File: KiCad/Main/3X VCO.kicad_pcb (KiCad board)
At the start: 2 copper layers, 99.6 x 99.8 mm, 92 parts, among them J1 Conn_01x32_Socket, J2 Conn_02x05_Odd_Even, J3 Conn_01x32_Socket, Q1 BC558, Q2 BC548, Q3 BC558, Q4 BC548, Q5 BC558, Q6 BC548, U1 40106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

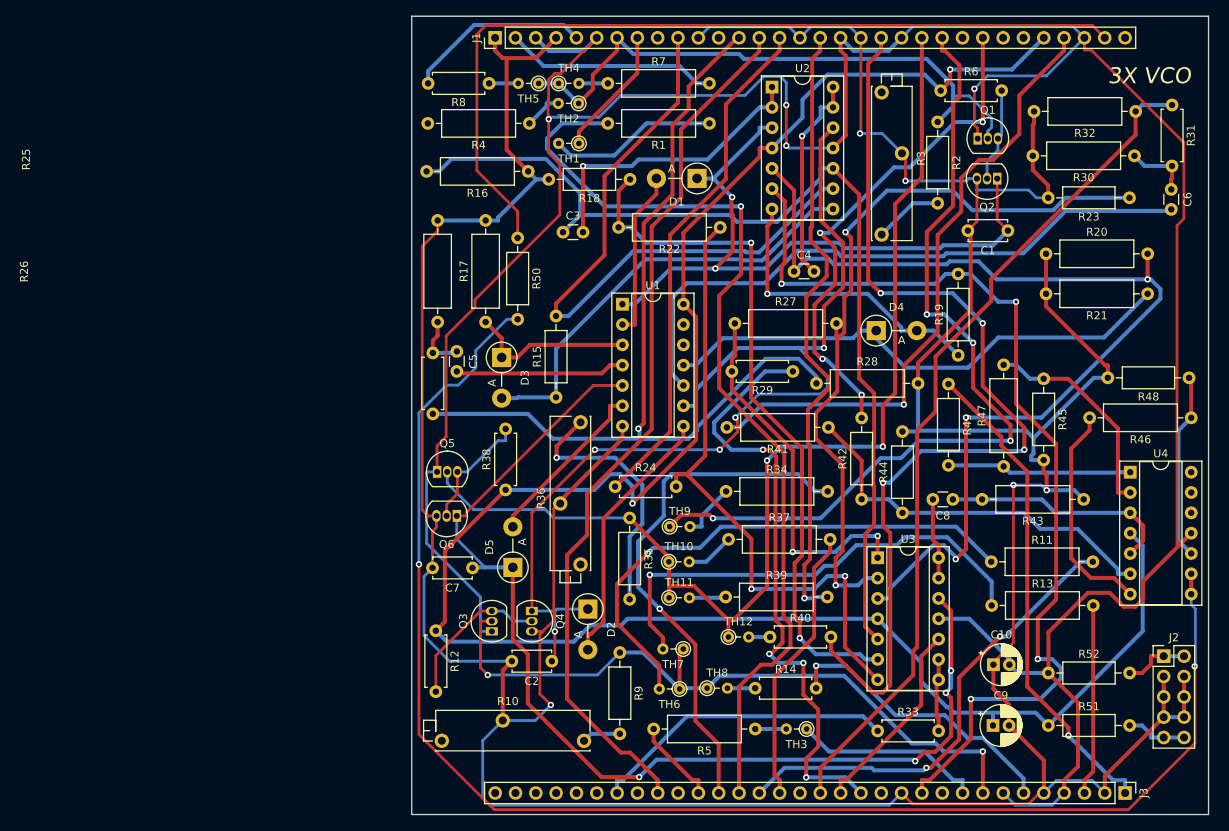
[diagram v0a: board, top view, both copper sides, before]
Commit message: updated main board PCB file, there were some unconnected pins
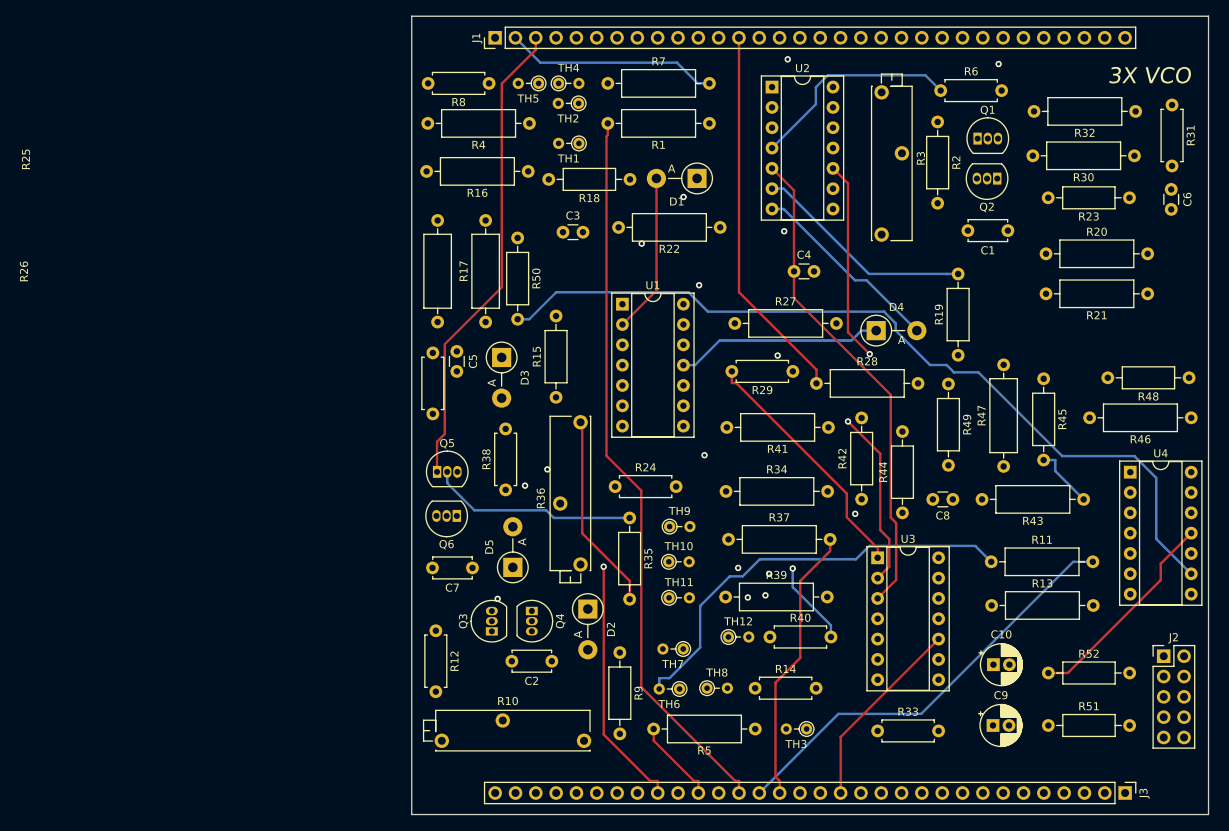
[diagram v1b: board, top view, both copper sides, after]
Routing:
- net cvIn1: track 0.00 -> 143.7 mm, vias 0 -> 1
- net SW2p2: track 0.00 -> 136.5 mm, vias 0 -> 1
- net VCO2PwmPot2: track 0.00 -> 111.8 mm
- net Net-(U4C--): track 184.4 -> 107.7 mm, vias 2 -> 0
- net VCO1CoarsePot1: track 502.9 -> 430.7 mm, vias 5 -> 0
- net Net-(D2-K): track 129.1 -> 92.0 mm, vias 5 -> 1
- net Net-(D5-K): track 135.8 -> 99.7 mm, vias 4 -> 0
- net VCO2FinePot2: track 122.2 -> 86.1 mm, vias 4 -> 1
- net VCO2IDKPot2: track 78.5 -> 109.6 mm, vias 1 -> 0
- net VCO1CoarsePot3: track 358.8 -> 329.4 mm, vias 4 -> 0
- net fmIn1: track 118.6 -> 90.9 mm, vias 1 -> 0
- net VCO3PwmPot1: track 123.5 -> 98.5 mm, vias 4 -> 0
- net fmIn2: track 66.2 -> 43.4 mm, vias 1 -> 0
- net VCO2FMPot2: track 106.2 -> 84.9 mm, vias 4 -> 2
- net VCO1PwmPot1: track 82.4 -> 64.4 mm, vias 0 -> 1
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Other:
- copper layers 2 -> 4
